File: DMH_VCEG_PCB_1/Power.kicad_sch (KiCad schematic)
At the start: 14 parts, among them J0 Conn_01x01, J100 IDC_02x05, J101 IDC_02x08

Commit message: Initiated schematic design
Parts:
- removed C5: 47uF, Capacitor_THT:CP_Radial_D4.0mm_P1.50mm, symbol Device:C_Polarized
- removed C6: 100nF, Capacitor_THT:C_Disc_D4.3mm_W1.9mm_P5.00mm, symbol Device:C
- removed D1, D5: SB140+, Diode_THT:D_DO-41_SOD81_P10.16mm_Horizontal, symbol SynthStuff:Power_Bus_Schotty_+
- removed D2: SB140-, Diode_THT:D_DO-41_SOD81_P10.16mm_Horizontal, symbol SynthStuff:Power_Bus_Schotty_-
- removed J100: IDC_02x05, SynthStuff:IDC-Header_2x05_P2.54mm_Vertical_Eurorack, symbol SynthStuff:Eurorack_Power_Connector_10Pin
- renumbered J101 to J100
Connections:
- net at J100.6a (Pin_6a): no longer J100.6b (Pin_6b)
- net Bus CV: no longer names the net of J100.7a (Pin_7a)
- net Bus CV: no longer J100.7b (Pin_7b)
- no-connect marks 0 -> 4
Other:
- note removed: "Delete what's not needed!"

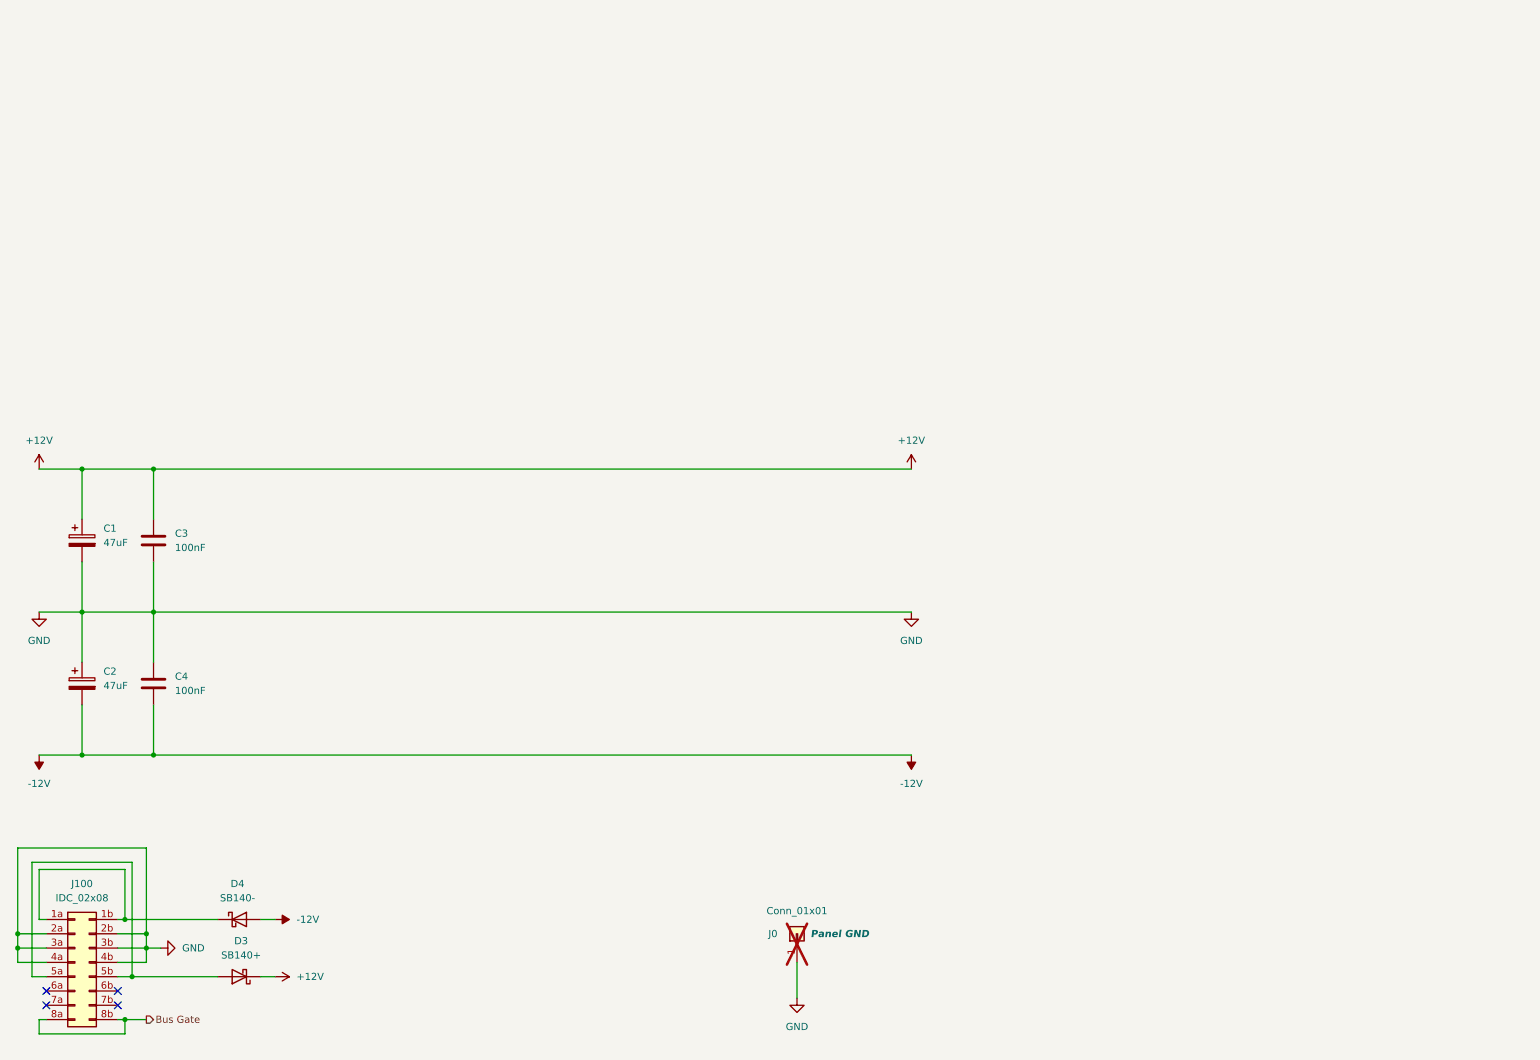
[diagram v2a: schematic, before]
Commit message: Core Circuit A ready for breadboarding
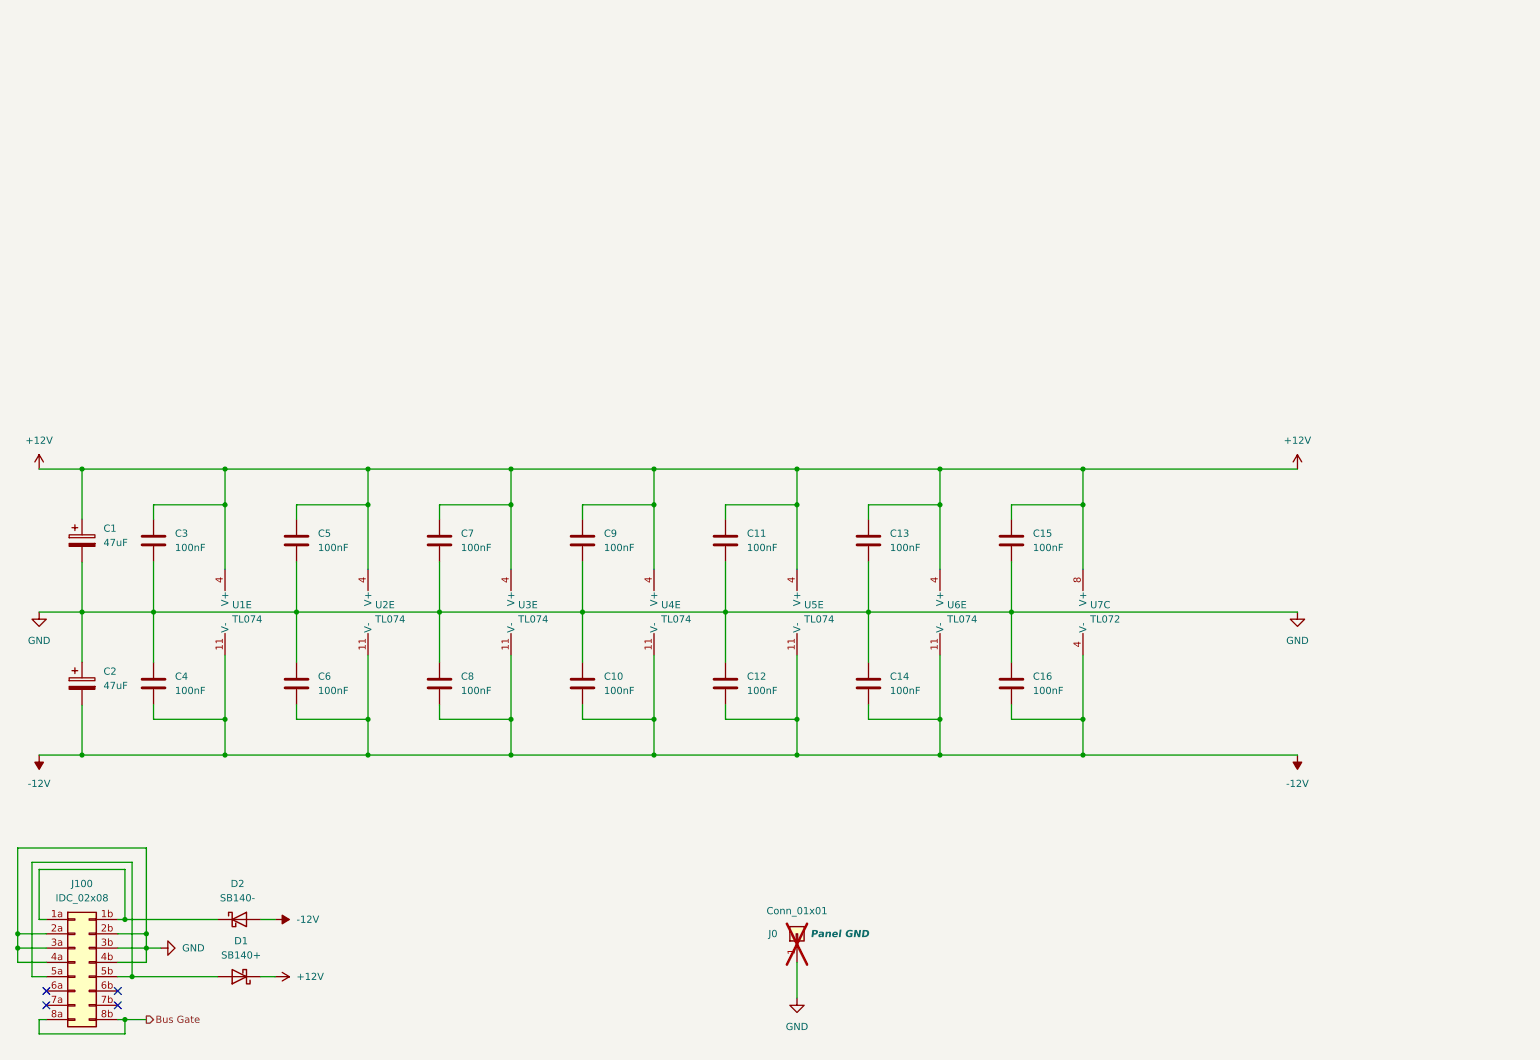
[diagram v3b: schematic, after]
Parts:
- added C10, C11, C12, C13, C14, C15, C16, C5, C6, C7, C8, C9: 100nF, Capacitor_THT:C_Disc_D4.3mm_W1.9mm_P5.00mm, symbol Device:C
- added U1, U2, U3, U4, U5, U6: TL074, symbol Amplifier_Operational:TL074
- added U7: TL072, symbol Amplifier_Operational:TL072
- renumbered D3 to D1, D4 to D2
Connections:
- net +12V: now also C11.1, C13.1, C15.1, C5.1, C7.1, C9.1, U1.4 (V+), U2.4 (V+), U3.4 (V+), U4.4 (V+), U5.4 (V+), U6.4 (V+), U7.8 (V+)
- net -12V: now also C10.2, C12.2, C14.2, C16.2, C6.2, C8.2, U1.11 (V-), U2.11 (V-), U3.11 (V-), U4.11 (V-), U5.11 (V-), U6.11 (V-), U7.4 (V-)
- net GND: now also C10.1, C11.2, C12.1, C13.2, C14.1, C15.2, C16.1, C5.2, C6.1, C7.2, C8.1, C9.2

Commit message: Minor corrections during breadboarding
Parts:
- U1, U2, U3, U4, U5, U6: footprint (none) -> Package_DIP:DIP-14_W7.62mm_Socket
- U7: footprint (none) -> Package_DIP:DIP-8_W7.62mm_Socket
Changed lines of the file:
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@@
 			)
 		)
-		(property "Footprint" ""
+		(property "Footprint" "Package_DIP:DIP-14_W7.62mm_Socket"
 			(at 153.67 118.11 0)
 			(effects
@@
 			)
 		)
-		(property "Footprint" ""
+		(property "Footprint" "Package_DIP:DIP-14_W7.62mm_Socket"
 			(at 128.27 118.11 0)
 			(effects
@@
 			)
 		)
-		(property "Footprint" ""
+		(property "Footprint" "Package_DIP:DIP-14_W7.62mm_Socket"
 			(at 179.07 118.11 0)
 			(effects
@@
 			)
 		)
-		(property "Footprint" ""
+		(property "Footprint" "Package_DIP:DIP-14_W7.62mm_Socket"
 			(at 102.87 118.11 0)
 			(effects
@@
 				)
 				(hide yes)
+			)
+		)
+		(property "Function" ""
+			(at 104.14 120.65 0)
+			(effects
+				(font
+					(size 1.27 1.27)
+				)
 			)
 		)
@@
 			)
 		)
-		(property "Footprint" ""
+		(property "Footprint" "Package_DIP:DIP-8_W7.62mm_Socket"
 			(at 205.74 120.65 0)
 			(effects
@@
 			)
 		)
-		(property "Footprint" ""
+		(property "Footprint" "Package_DIP:DIP-14_W7.62mm_Socket"
 			(at 52.07 118.11 0)
 			(effects
@@
 			)
 		)
-		(property "Footprint" ""
+		(property "Footprint" "Package_DIP:DIP-14_W7.62mm_Socket"
 			(at 77.47 118.11 0)
 			(effects

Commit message: MFOS based core circuit in progress
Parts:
- renumbered U5 to U?, U4 to U?, U6 to U?, U3 to U?, U7 to U?, U1 to U?, U2 to U?
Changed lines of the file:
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@@
 		(dnp no)
 		(fields_autoplaced yes)
-		(property "Reference" "U5"
+		(property "Reference" "U?"
 			(at 153.67 119.3799 0)
 			(effects
@@
 			(project ""
 				(path "/58f4306d-5387-4983-bb08-41a2313fd315/0cdf34b2-39cd-4d9e-981a-97cd34791509"
-					(reference "U5")
+					(reference "U?")
 					(unit 5)
 				)
@@
 		(dnp no)
 		(fields_autoplaced yes)
-		(property "Reference" "U4"
+		(property "Reference" "U?"
 			(at 128.27 119.3799 0)
 			(effects
@@
 			(project ""
 				(path "/58f4306d-5387-4983-bb08-41a2313fd315/0cdf34b2-39cd-4d9e-981a-97cd34791509"
-					(reference "U4")
+					(reference "U?")
 					(unit 5)
 				)
@@
 		(dnp no)
 		(fields_autoplaced yes)
-		(property "Reference" "U6"
+		(property "Reference" "U?"
 			(at 179.07 119.3799 0)
 			(effects
@@
 			(project "DMH_VCEG_PCB_1"
 				(path "/58f4306d-5387-4983-bb08-41a2313fd315/0cdf34b2-39cd-4d9e-981a-97cd34791509"
-					(reference "U6")
+					(reference "U?")
 					(unit 5)
 				)
@@
 		(dnp no)
 		(fields_autoplaced yes)
-		(property "Reference" "U3"
+		(property "Reference" "U?"
 			(at 102.87 119.3799 0)
 			(effects
@@
 			(project ""
 				(path "/58f4306d-5387-4983-bb08-41a2313fd315/0cdf34b2-39cd-4d9e-981a-97cd34791509"
-					(reference "U3")
+					(reference "U?")
 					(unit 5)
 				)
@@
 		(dnp no)
 		(fields_autoplaced yes)
-		(property "Reference" "U7"
+		(property "Reference" "U?"
 			(at 204.47 119.3799 0)
 			(effects
@@
 			(project ""
 				(path "/58f4306d-5387-4983-bb08-41a2313fd315/0cdf34b2-39cd-4d9e-981a-97cd34791509"
-					(reference "U7")
+					(reference "U?")
 					(unit 3)
 				)
@@
 		(dnp no)
 		(fields_autoplaced yes)
-		(property "Reference" "U1"
+		(property "Reference" "U?"
 			(at 52.07 119.3799 0)
 			(effects
@@
 			(project ""
 				(path "/58f4306d-5387-4983-bb08-41a2313fd315/0cdf34b2-39cd-4d9e-981a-97cd34791509"
-					(reference "U1")
+					(reference "U?")
 					(unit 5)
 				)
@@
 		(dnp no)
 		(fields_autoplaced yes)
-		(property "Reference" "U2"
+		(property "Reference" "U?"
 			(at 77.47 119.3799 0)
 			(effects
@@
 			(project ""
 				(path "/58f4306d-5387-4983-bb08-41a2313fd315/0cdf34b2-39cd-4d9e-981a-97cd34791509"
-					(reference "U2")
+					(reference "U?")
 					(unit 5)
 				)

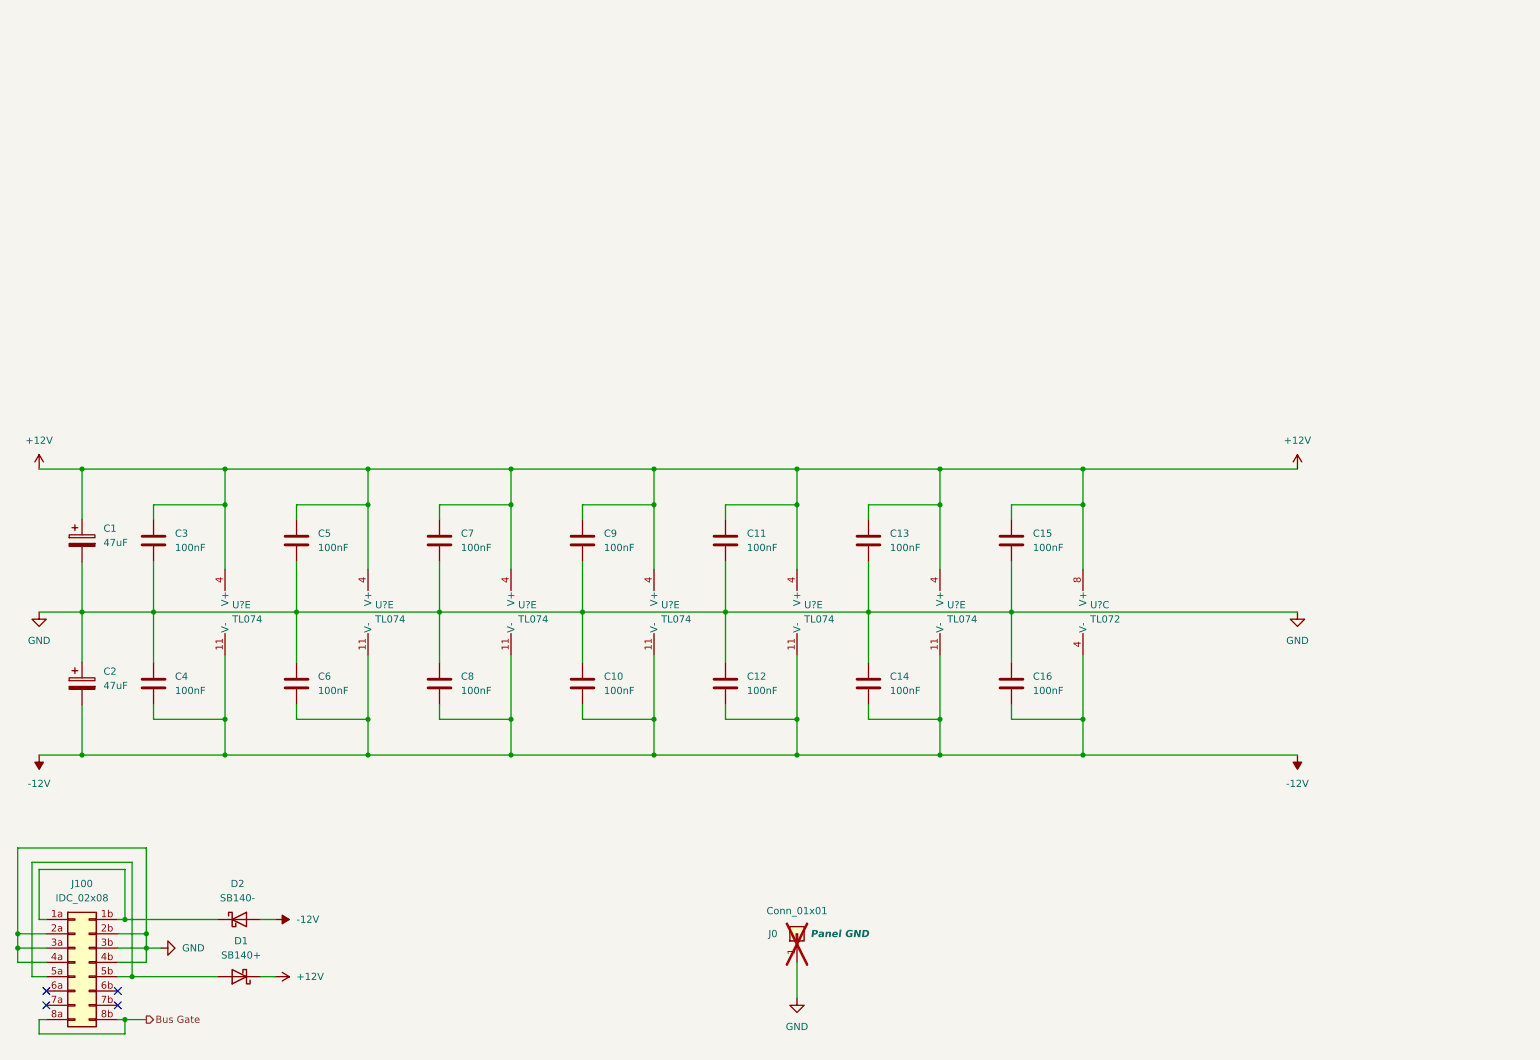
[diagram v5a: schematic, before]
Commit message: Corrected Out R design
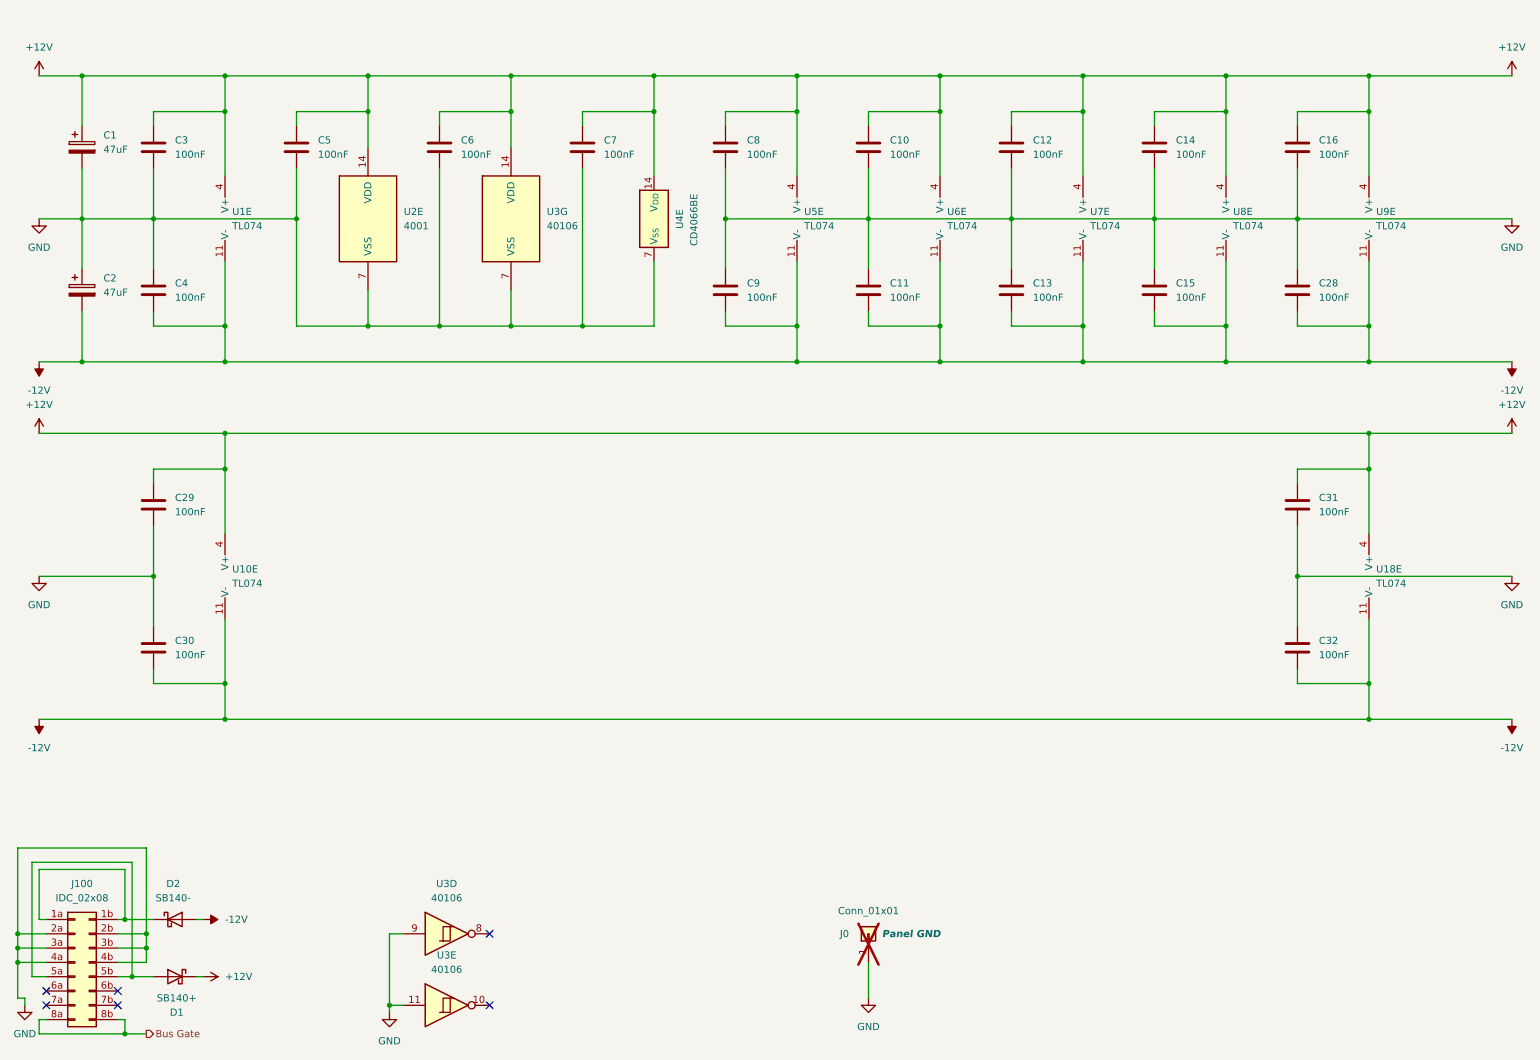
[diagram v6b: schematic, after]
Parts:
- removed C15, C16: 100nF, Capacitor_THT:C_Disc_D4.3mm_W1.9mm_P5.00mm, symbol Device:C
- removed U?: TL072, Package_DIP:DIP-8_W7.62mm_Socket, symbol Amplifier_Operational:TL072
- added C29, C30, C31, C32, C5, C6, C7: 100nF, Capacitor_THT:C_Disc_D4.3mm_W1.9mm_P5.00mm, symbol Device:C
- added U10: TL074, Package_DIP:DIP-14_W7.62mm_Socket, symbol Amplifier_Operational:TL074
- added U18: TL074, symbol Amplifier_Operational:TL074
- added U2: 4001, symbol 4xxx:4001
- added U3: 40106, symbol 4xxx:40106
- added U4: CD4066BE, Package_DIP:DIP-14_W7.62mm, symbol Analog_Switch:CD4066BE
- U1: renamed from U?; footprint Package_DIP:DIP-14_W7.62mm_Socket -> (none)
- gave numbers to parts that had none: 5
- renumbered C7 to C10, C8 to C11, C9 to C12, C10 to C13, C11 to C14, C12 to C15, C13 to C16, C14 to C28, C5 to C8, C6 to C9
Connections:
- net +12V: now also C29.1, C31.1, C5.1, C6.1, C7.1, U10.4 (V+), U18.4 (V+), U2.14 (VDD), U3.14 (VDD), U4.14 (V_{DD})
- net -12V: now also C30.2, C32.2, U10.11 (V-), U18.11 (V-)
- net GND: now also C29.2, C30.1, C31.2, C32.1, C5.2, C6.2, C7.2, U2.7 (VSS), U3.11, U3.7 (VSS), U3.9, U4.7 (V_{SS})
- no-connect marks 4 -> 6
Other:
- moved on the sheet: C1, C10, C11, C12, C13, C14, C15, C16, C2, C28, C3, C4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

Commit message: Reanotated schematic
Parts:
- added C30, C32, C34, C37, C38, C41, C42, C45, C46, C49, C50: 100nF, Capacitor_THT:C_Disc_D4.3mm_W1.9mm_P5.00mm, symbol Device:C
- added U11, U14, U5, U9: TL074, Package_DIP:DIP-14_W7.62mm_Socket, symbol Amplifier_Operational:TL074
- added U13: CD4066BE, Package_DIP:DIP-14_W7.62mm, symbol Analog_Switch:CD4066BE
- added U15: 40106, Package_DIP:DIP-14_W7.62mm_Socket, symbol 4xxx:40106
- added U16: 4001, Package_DIP:DIP-14_W7.62mm_Socket, symbol 4xxx:4001
- U1, U18: footprint (none) -> Package_DIP:DIP-14_W7.62mm_Socket
- U6: renamed from U3; footprint (none) -> Package_DIP:DIP-14_W7.62mm_Socket
- U7: renamed from U2; footprint (none) -> Package_DIP:DIP-14_W7.62mm_Socket
- renumbered C1 to C23, C2 to C24, C3 to C25, C4 to C26, C29 to C27, C30 to C28, C5 to C29, C6 to C31, C7 to C33, C8 to C35, C9 to C36, C10 to C39, C11 to C40, C12 to C43, C13 to C44, C14 to C47, C15 to C48, C16 to C51, C28 to C52, C31 to C53, C32 to C54, D2 to D1, D1 to D2, U7 to U10, U8 to U12, U9 to U17, U10 to U2, U5 to U3, U6 to U8
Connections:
- net +12V: now also C30.1, C32.1, C34.1, C37.1, C41.1, C45.1, C49.1, U11.4 (V+), U13.14 (V_{DD}), U14.4 (V+), U15.14 (VDD), U16.14 (VDD), U5.4 (V+), U9.4 (V+)
- net -12V: now also C38.2, C42.2, C46.2, C50.2, U11.11 (V-), U14.11 (V-), U5.11 (V-), U9.11 (V-)
- net GND: now also C30.2, C32.2, C34.2, C37.2, C38.1, C41.2, C42.1, C45.2, C46.1, C49.2, C50.1, U13.7 (V_{SS}), U15.11, U15.7 (VSS), U15.9, U16.7 (VSS)
- no-connect marks 6 -> 8
